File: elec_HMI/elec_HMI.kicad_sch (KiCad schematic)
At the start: 33 parts, among them J1 JST SH, J2 JST SH, SW1 SW_SPST, SW2 SW_SPST, U1 PCF8574ATS

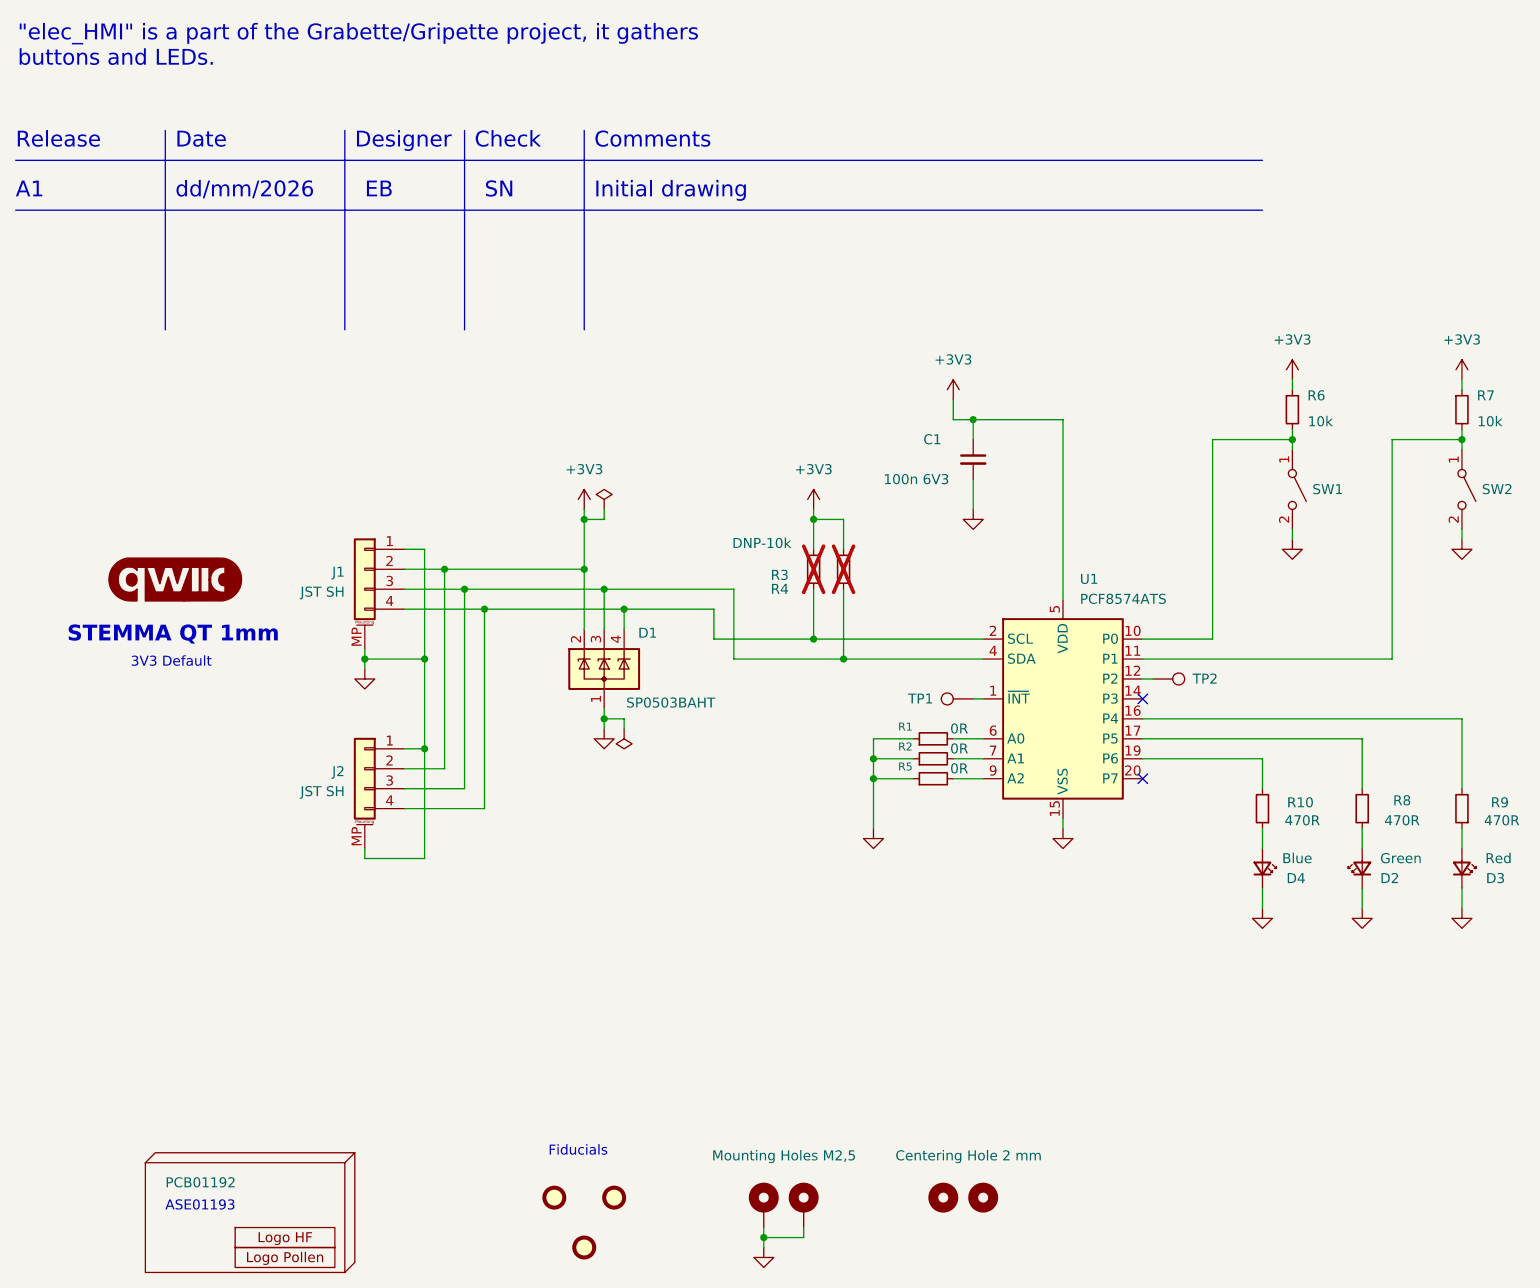
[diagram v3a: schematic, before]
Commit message: [update] Mechanical adaptations.
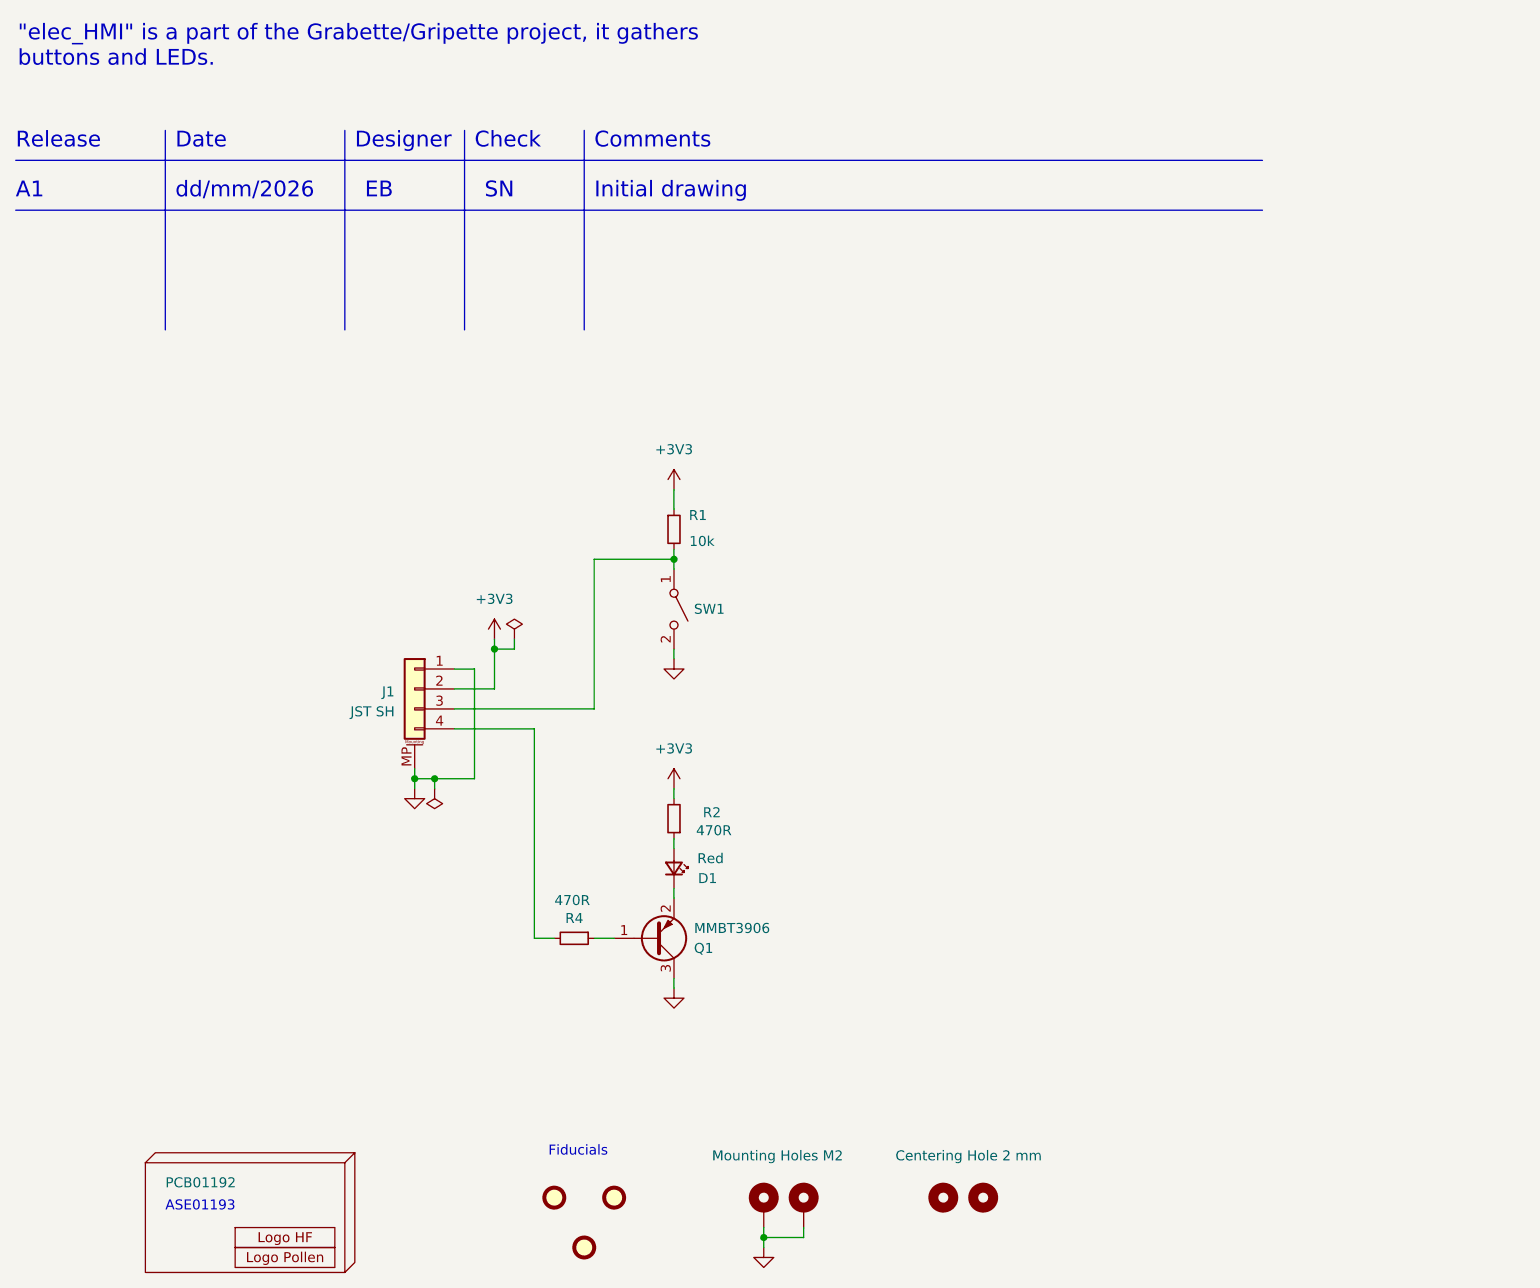
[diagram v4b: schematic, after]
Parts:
- removed C1: 100n 6V3, Capacitor_SMD:C_0402_1005Metric, symbol Device:C_Small
- removed D1: SP0503BAHT, Package_TO_SOT_SMD:SOT-143, symbol Power_Protection:SP0503BAHT
- removed D2: Green, LED_SMD:LED_0603_1608Metric, symbol Device:LED_Small
- removed D4: Blue, LED_SMD:LED_0603_1608Metric, symbol Device:LED_Small
- removed G1: qwiic_Logo, Library_Pollen:Logo_qwiic_5mm, symbol Library_Pollen:Logo qwiic
- removed J2: JST SH, Connector_JST:JST_SH_SM04B-SRSS-TB_1x04-1MP_P1.00mm_Horizontal, symbol Connector_Generic_MountingPin:Conn_01x04_MountingPin
- removed R1, R2, R5: 0R, Resistor_SMD:R_0402_1005Metric, symbol Device:R_Small
- removed R10, R8: 470R, Resistor_SMD:R_0402_1005Metric, symbol Device:R_Small
- removed R3: DNP-10k, Resistor_SMD:R_0402_1005Metric, symbol Device:R_Small
- removed R7: 10k, Resistor_SMD:R_0402_1005Metric, symbol Device:R_Small
- removed SW2: SW_SPST, Button_Switch_Keyboard:SW_Cherry_MX_1.00u_PCB, symbol Switch:SW_SPST
- removed TP1, TP2: TestPoint, TestPoint:TestPoint_Loop_D2.50mm_Drill1.0mm_LowProfile, symbol Connector:TestPoint
- removed U1: PCF8574ATS, Package_SO:SSOP-20_4.4x6.5mm_P0.65mm, symbol Interface_Expansion:PCF8574ATS
- added Q1: MMBT3906, Package_TO_SOT_SMD:SOT-23, symbol Transistor_BJT:MMBT3906
- H4: value Mounting Holes M2,5 -> Mounting Holes M2; footprint MountingHole:MountingHole_2.7mm_M2.5_ISO7380_Pad_TopBottom -> MountingHole:MountingHole_2.2mm_M2_ISO7380_Pad_TopBottom
- H5: value MountingHole_Pad -> Mounting Holes M2; footprint MountingHole:MountingHole_2.7mm_M2.5_ISO7380_Pad_TopBottom -> MountingHole:MountingHole_2.2mm_M2_ISO7380_Pad_TopBottom
- R4: value DNP-10k -> 470R; LCSC Part C25744 -> C25117; now fitted
- SW1: footprint Button_Switch_Keyboard:SW_Cherry_MX_1.00u_PCB -> LCSC_parts_lib:KEY-TH_CPG135001D0X; LCSC Part (none) -> C400229
- renumbered D3 to D1, R6 to R1, R9 to R2
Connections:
- net +3V3: now also R2.2; no longer R4.1
- net GND: now also Q1.3 (C); no longer D1.1 (K)
- net at J1.4 (Pin_4): now also R4.2
- net at R1.2, SW1.1 (A): now also J1.3 (Pin_3)
- new net: D1.1 (K), Q1.2 (E)
- new net: Q1.1 (B), R4.1
- no-connect marks 2 -> 0
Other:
- note removed: "3V3 Default"
- note removed: "STEMMA QT 1mm"
- moved on the sheet: D1, J1, R1, R2, SW1

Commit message: [update] OK for JLC
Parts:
- SW1: FT Position Offset (none) -> 2.5,2.3
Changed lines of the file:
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@@
+			)
+		)
+		(property "FT Position Offset" "2.5,2.3"
+			(at 102.87 96.52 90)
+			(effects
+				(font
+					(size 1.27 1.27)
+				)
+				(hide yes)
 			)
 		)

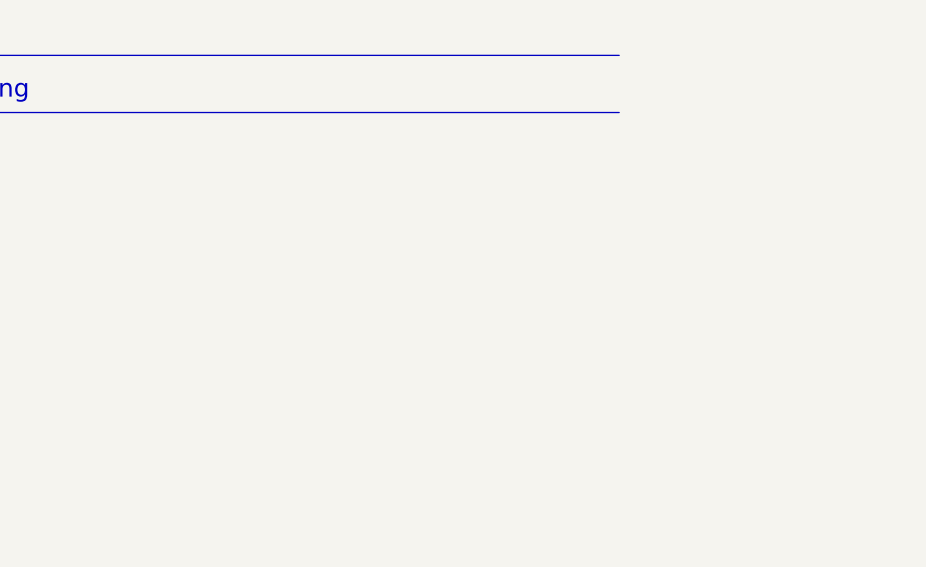
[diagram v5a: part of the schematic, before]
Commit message: [update] Gripette hub routed
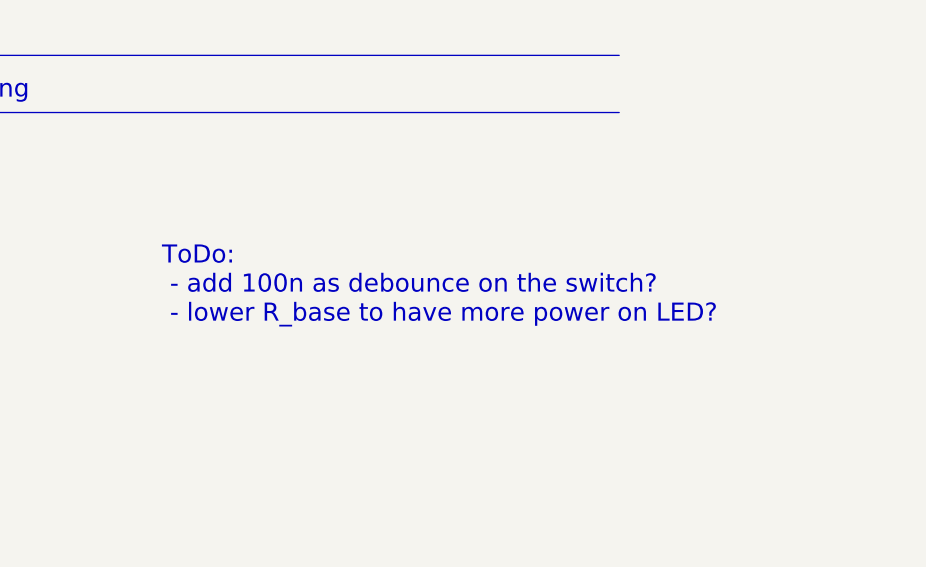
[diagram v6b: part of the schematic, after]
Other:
- note added: "ToDo: - add 100n as debounce on the switch? - lower R_base to have more power on LED?"
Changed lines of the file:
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@@
+		)
+	)
+	(text "ToDo:\n - add 100n as debounce on the switch?\n - lower R_base to have more power on LED?"
+		(exclude_from_sim no)
+		(at 127 69.342 0)
+		(effects
+			(font
+				(size 2.0066 2.0066)
+			)
+			(justify left bottom)
 		)
 	)
